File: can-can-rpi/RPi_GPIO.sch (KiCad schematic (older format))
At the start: 1 part, among them J2 RPi_GPIO

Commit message: wip
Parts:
- added C1, C2, C5, C6, C7: 100nF, Capacitors_ThroughHole:C_Disc_D3_P2.5, symbol C
- added C3, C4: 27pF, Capacitors_ThroughHole:C_Disc_D3_P2.5, symbol C
- added CON1: BARREL_JACK, Connect:BARREL_JACK, symbol BARREL_JACK
- added JP1: ICSP, ICSP:ICSP, symbol ICSP
- added JP2, JP3, JP4, JP5, JP6: JUMPER, Wire_Pads:SolderWirePad_2x_1mmDrill, symbol JUMPER
- added OC1, OC2: 6N137, Housings_DIP:DIP-8_W7.62mm, symbol 6N137
- added P1: CONN_02X02, Pin_Headers:Pin_Header_Straight_2x02, symbol CONN_02X02
- added P2, P3: CONN_01X14, Socket_Strips:Socket_Strip_Straight_1x14, symbol CONN_01X14
- added P5: CONN_01X03, Pin_Headers:Pin_Header_Straight_1x03, symbol CONN_01X03
- added R1: 15k, Resistors_ThroughHole:Resistor_Horizontal_RM10mm, symbol R
- added R10, R7, R8, R9: 390, Resistors_ThroughHole:Resistor_Horizontal_RM10mm, symbol R
- added R3, R4: 3k3, Resistors_ThroughHole:Resistor_Horizontal_RM10mm, symbol R
- added R5, R6: 470, Resistors_ThroughHole:Resistor_Horizontal_RM10mm, symbol R
- added U1: PIC18F25K80, Housings_DIP:DIP-28_W7.62mm, symbol PIC18F25K80
- added U2: MCP2562-I/P, Housings_DIP:DIP-8_W7.62mm_LongPads, symbol MCP2562-I/P
- added Y1: 16MHz, Crystals:Crystal_HC49-U_Vertical, symbol Crystal
- J1: renamed from J2; footprint RPi_Hat:Pin_Header_Straight_2x20 -> Socket_Strips:Socket_Strip_Straight_2x20
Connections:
- net labels added: +5V, CANRX, CANTX, GND, GNDA, PGC, PGD, RA0, RA1, RA2, RA3, RA5, RA6, RA7, RB0, RB1, RB4, RB5, RC0, RC1, RC2, RC5, RxD, SCL, SDA, TxD, VCC, VDD, _CANRX, _CANTX, ~MCLR
- wire segments 0 -> 174
- no-connect marks 0 -> 25
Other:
- note added: "Bypass galvanic isolation\n"
- moved on the sheet: J1

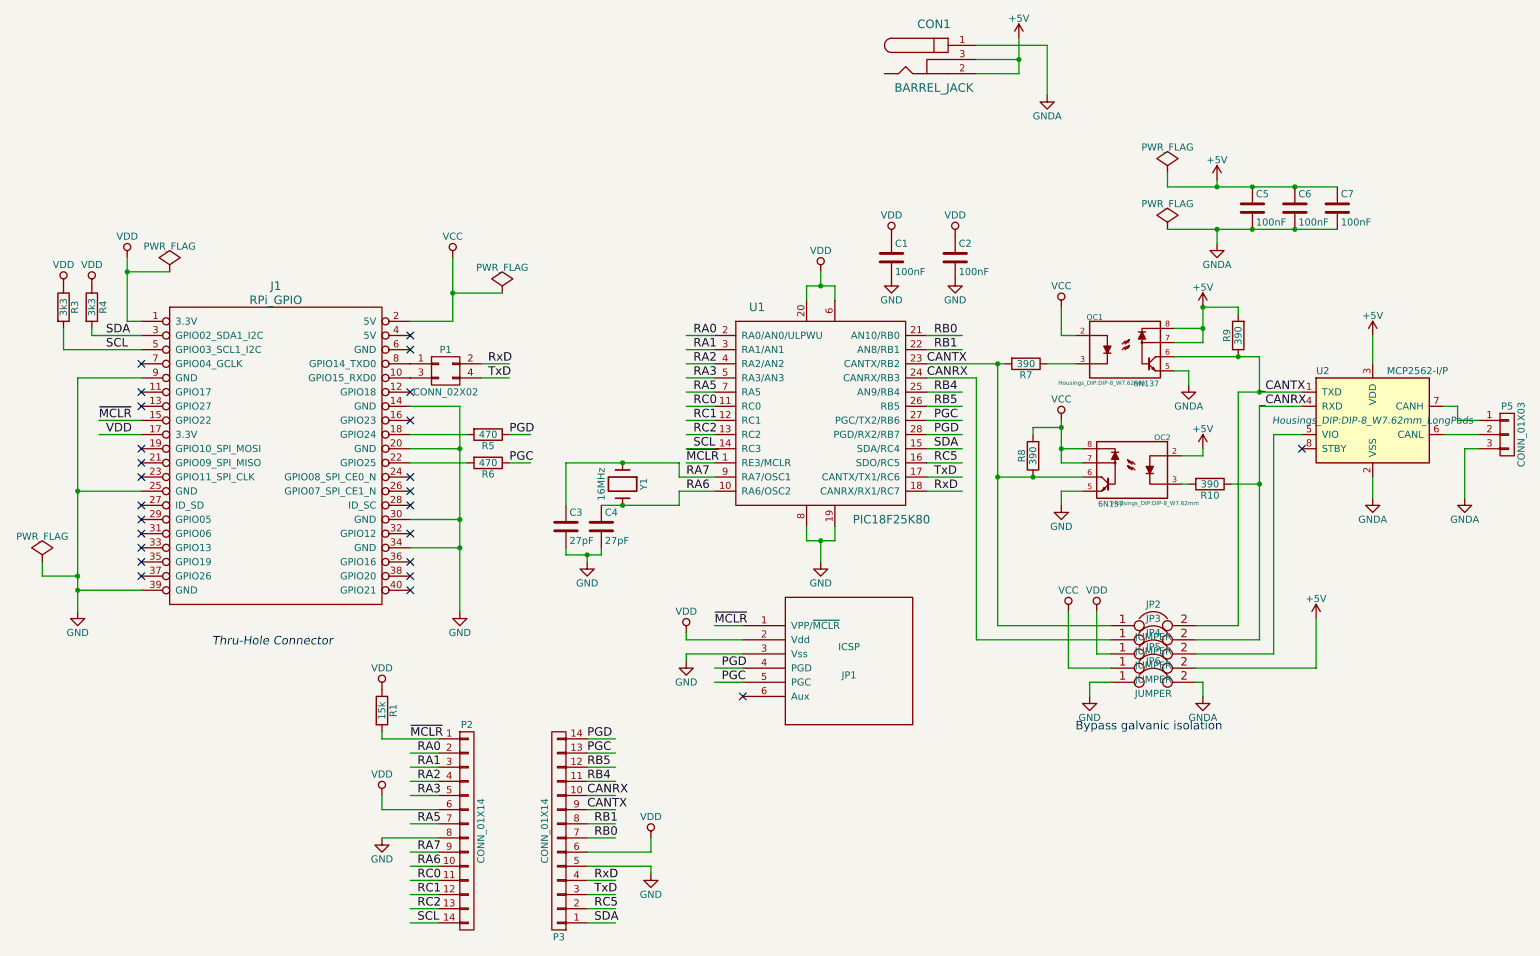
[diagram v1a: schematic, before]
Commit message: add LEDs and CTS
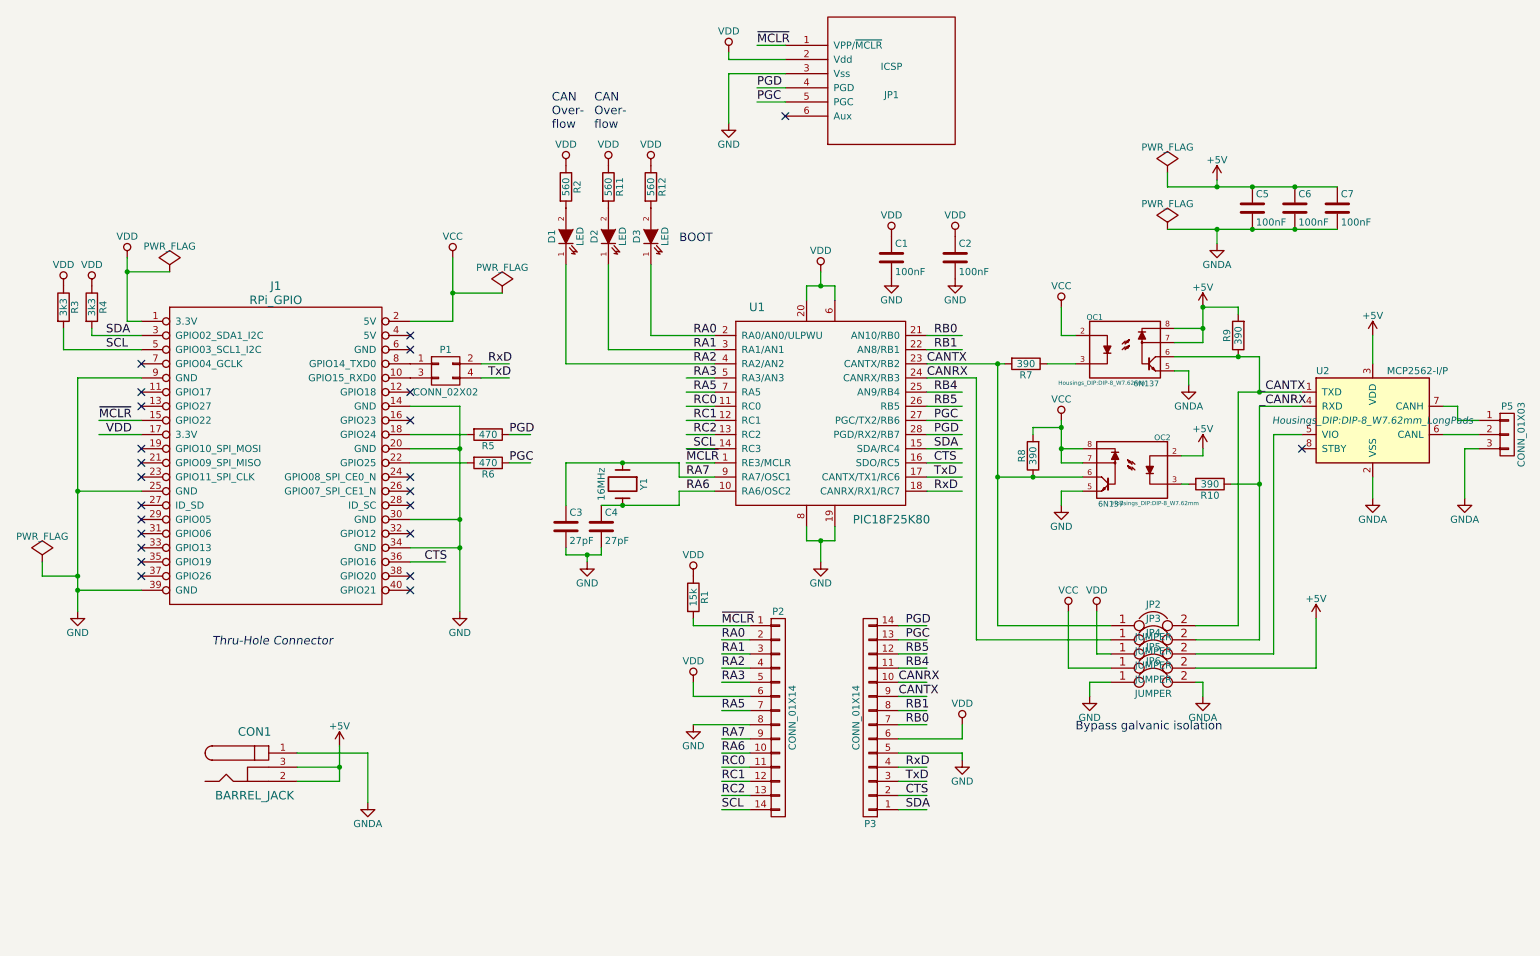
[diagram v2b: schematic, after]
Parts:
- added D1, D2, D3: LED, symbol LED
- added R11, R12, R2: 560, Resistors_ThroughHole:Resistor_Horizontal_RM10mm, symbol R
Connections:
- net labels added: CTS
- net labels removed: RC5
- wire segments 174 -> 178
- no-connect marks 25 -> 24
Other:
- note added: "BOOT"
- note added: "CAN\nOver-\nflow"
- moved on the sheet: CON1, JP1, P2, P3, R1

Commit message: update schematic and board
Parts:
- added P4: CONN_01X02, Pin_Headers:Pin_Header_Straight_1x02, symbol CONN_01X02
- added R13: 120, Resistors_ThroughHole:Resistor_Horizontal_RM10mm, symbol R
- added R14: 680, Resistors_ThroughHole:Resistor_Horizontal_RM10mm, symbol R
- D1, D2, D3: footprint (none) -> LEDs:LED-3MM
- R5, R6: value 470 -> 390
- R7: value 390 -> 180
- renumbered R2 to R12, R12 to R2
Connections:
- no-connect marks 24 -> 26
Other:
- moved on the sheet: R5, R6
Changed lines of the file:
@@
 EESchema Schematic File Version 2
+LIBS:RPi_Hat-rescue
 LIBS:power
 LIBS:device
@@
 $EndComp
 $Comp
-L GND #PWR01
+L GND-RESCUE-RPi_Hat #PWR01
 U 1 1 55BB6A0A
 P 6200 4550
+AR Path="/55BB6A0A" Ref="#PWR01"  Part="1"
+AR Path="/5515D395/55BB6A0A" Ref="#PWR01"  Part="1"
 F 0 "#PWR01" H 6200 4300 50  0001 C CNN
 F 1 "GND" H 6200 4400 50  0000 C CNN
@@
 $EndComp
 $Comp
-L GND #PWR03
+L GND-RESCUE-RPi_Hat #PWR03
 U 1 1 55BB6AF3
 P 6700 2550
+AR Path="/55BB6AF3" Ref="#PWR03"  Part="1"
+AR Path="/5515D395/55BB6AF3" Ref="#PWR03"  Part="1"
 F 0 "#PWR03" H 6700 2300 50  0001 C CNN
 F 1 "GND" H 6700 2400 50  0000 C CNN
@@
 $EndComp
 $Comp
-L GND #PWR05
+L GND-RESCUE-RPi_Hat #PWR05
 U 1 1 55BB6C16
 P 7150 2550
+AR Path="/55BB6C16" Ref="#PWR05"  Part="1"
+AR Path="/5515D395/55BB6C16" Ref="#PWR05"  Part="1"
 F 0 "#PWR05" H 7150 2300 50  0001 C CNN
 F 1 "GND" H 7150 2400 50  0000 C CNN
@@
 $EndComp
 $Comp
-L GND #PWR07
+L GND-RESCUE-RPi_Hat #PWR07
 U 1 1 55BB6F4C
 P 4550 4550
+AR Path="/55BB6F4C" Ref="#PWR07"  Part="1"
+AR Path="/5515D395/55BB6F4C" Ref="#PWR07"  Part="1"
 F 0 "#PWR07" H 4550 4300 50  0001 C CNN
 F 1 "GND" H 4550 4400 50  0000 C CNN
@@
 	1    0    0    -1
 $EndComp
-Text Label 3850 3150 0    60   ~ 0
-RxD
-Text Label 3850 3250 0    60   ~ 0
-TxD
 $Comp
 L 6N137 OC1
@@
 $EndComp
 $Comp
-L GND #PWR012
+L GND-RESCUE-RPi_Hat #PWR012
 U 1 1 55BBE7FB
 P 7200 5950
+AR Path="/55BBE7FB" Ref="#PWR012"  Part="1"
+AR Path="/5515D395/55BBE7FB" Ref="#PWR012"  Part="1"
 F 0 "#PWR012" H 7200 5700 50  0001 C CNN
 F 1 "GND" H 7200 5800 50  0000 C CNN
@@
 $EndComp
 $Comp
-L GND #PWR016
+L GND-RESCUE-RPi_Hat #PWR016
 U 1 1 55BC19FE
 P 5300 5700
+AR Path="/55BC19FE" Ref="#PWR016"  Part="1"
+AR Path="/5515D395/55BC19FE" Ref="#PWR016"  Part="1"
 F 0 "#PWR016" H 5300 5450 50  0001 C CNN
 F 1 "GND" H 5300 5550 50  0000 C CNN
@@
 $EndComp
 $Comp
-L GND #PWR019
+L GND-RESCUE-RPi_Hat #PWR019
 U 1 1 55BC3BB4
 P 3650 4900
+AR Path="/55BC3BB4" Ref="#PWR019"  Part="1"
+AR Path="/5515D395/55BC3BB4" Ref="#PWR019"  Part="1"
 F 0 "#PWR019" H 3650 4650 50  0001 C CNN
 F 1 "GND" H 3650 4750 50  0000 C CNN
@@
 $EndComp
 $Comp
-L GND #PWR020
+L GND-RESCUE-RPi_Hat #PWR020
 U 1 1 55BC413C
 P 950 4900
+AR Path="/55BC413C" Ref="#PWR020"  Part="1"
+AR Path="/5515D395/55BC413C" Ref="#PWR020"  Part="1"
 F 0 "#PWR020" H 950 4650 50  0001 C CNN
 F 1 "GND" H 950 4750 50  0000 C CNN
@@
 $EndComp
 $Comp
-L GNDA #PWR023
+L GNDA-RESCUE-RPi_Hat #PWR023
 U 1 1 55BC53DA
 P 8800 3300
@@
 $EndComp
 $Comp
-L GND #PWR024
+L GND-RESCUE-RPi_Hat #PWR024
 U 1 1 55BC634B
-P 7900 4150
-F 0 "#PWR024" H 7900 3900 50  0001 C CNN
-F 1 "GND" H 7900 4000 50  0000 C CNN
-F 2 "" H 7900 4150 60  0000 C CNN
-F 3 "" H 7900 4150 60  0000 C CNN
-	1    7900 4150
+P 7900 4350
+AR Path="/55BC634B" Ref="#PWR024"  Part="1"
+AR Path="/5515D395/55BC634B" Ref="#PWR024"  Part="1"
+F 0 "#PWR024" H 7900 4100 50  0001 C CNN
+F 1 "GND" H 7900 4200 50  0000 C CNN
+F 2 "" H 7900 4350 60  0000 C CNN
+F 3 "" H 7900 4350 60  0000 C CNN
+	1    7900 4350
 	1    0    0    -1
 $EndComp
@@
 P 7650 3150
 F 0 "R7" V 7730 3150 50  0000 C CNN
-F 1 "390" V 7650 3150 50  0000 C CNN
+F 1 "180" V 7650 3150 50  0000 C CNN
 F 2 "Resistors_ThroughHole:Resistor_Horizontal_RM10mm" V 7580 3150 30  0001 C CNN
 F 3 "" H 7650 3150 30  0000 C CNN
@@
 L R R6
 U 1 1 55BCA023
-P 3850 3850
-F 0 "R6" V 3930 3850 50  0000 C CNN
-F 1 "470" V 3850 3850 50  0000 C CNN
-F 2 "Resistors_ThroughHole:Resistor_Horizontal_RM10mm" V 3780 3850 30  0001 C CNN
-F 3 "" H 3850 3850 30  0000 C CNN
-	1    3850 3850
+P 3950 3250
+F 0 "R6" V 4030 3250 50  0000 C CNN
+F 1 "390" V 3950 3250 50  0000 C CNN
+F 2 "Resistors_ThroughHole:Resistor_Horizontal_RM10mm" V 3880 3250 30  0001 C CNN
+F 3 "" H 3950 3250 30  0000 C CNN
+	1    3950 3250
 	0    1    1    0
 $EndComp
@@
 L R R5
 U 1 1 55BCA133
-P 3850 3650
-F 0 "R5" V 3930 3650 50  0000 C CNN
-F 1 "470" V 3850 3650 50  0000 C CNN
-F 2 "Resistors_ThroughHole:Resistor_Horizontal_RM10mm" V 3780 3650 30  0001 C CNN
-F 3 "" H 3850 3650 30  0000 C CNN
-	1    3850 3650
+P 3950 3150
+F 0 "R5" V 4030 3150 50  0000 C CNN
+F 1 "390" V 3950 3150 50  0000 C CNN
+F 2 "Resistors_ThroughHole:Resistor_Horizontal_RM10mm" V 3880 3150 30  0001 C CNN
+F 3 "" H 3950 3150 30  0000 C CNN
+	1    3950 3150
 	0    1    1    0
 $EndComp
-Text Label 4000 3650 0    60   ~ 0
+Text Label 4100 3150 0    60   ~ 0
 PGD
-Text Label 4000 3850 0    60   ~ 0
+Text Label 4100 3250 0    60   ~ 0
 PGC
 NoConn ~ 1400 3150
@@
 $EndComp
 $Comp
-L GNDA #PWR030
+L GNDA-RESCUE-RPi_Hat #PWR030
 U 1 1 55BCF91F
 P 9000 2300
@@
 $EndComp
 $Comp
-L GNDA #PWR033
+L GNDA-RESCUE-RPi_Hat #PWR033
 U 1 1 55BB9FC1
 P 10100 4100
@@
 Bypass galvanic isolation\n
 $Comp
-L GNDA #PWR035
+L GNDA-RESCUE-RPi_Hat #PWR035
 U 1 1 55BBBB99
 P 8900 5500
@@
 $EndComp
 $Comp
-L GND #PWR036
+L GND-RESCUE-RPi_Hat #PWR036
 U 1 1 55BBBC10
 P 8100 5500
+AR Path="/55BBBC10" Ref="#PWR036"  Part="1"
+AR Path="/5515D395/55BBBC10" Ref="#PWR036"  Part="1"
 F 0 "#PWR036" H 8100 5250 50  0001 C CNN
 F 1 "GND" H 8100 5350 50  0000 C CNN
@@
 $EndComp
 $Comp
-L GNDA #PWR037
+L GNDA-RESCUE-RPi_Hat #PWR037
 U 1 1 55BBC07E
 P 10750 4100
@@
 	6950 3950 7200 3950
 Wire Wire Line
-	3800 3150 4000 3150
-Wire Wire Line
-	3800 3250 4000 3250
-Wire Wire Line
 	1300 2850 1400 2850
 Wire Wire Line
@@
 	8050 4050 7900 4050
 Wire Wire Line
-	7900 4050 7900 4150
+	7900 4050 7900 4350
 Wire Wire Line
 	7800 3150 8000 3150
@@
 Wire Wire Line
 	1400 3550 1100 3550
-Wire Wire Line
-	3300 3850 3700 3850
-Wire Wire Line
-	3300 3650 3700 3650
-Wire Wire Line
-	4000 3650 4150 3650
-Wire Wire Line
-	4000 3850 4150 3850
 Wire Wire Line
 	9000 1850 9000 1900
@@
 Connection ~ 7450 3950
 Wire Wire Line
-	10600 3450 10700 3450
-Wire Wire Line
-	10700 3450 10700 3550
-Wire Wire Line
-	10700 3550 10850 3550
+	10600 3450 10600 3450
+Wire Wire Line
+	10600 3450 10600 3550
+Wire Wire Line
+	10600 3550 10850 3550
 Wire Wire Line
 	10850 3650 10600 3650
@@
 $EndComp
 $Comp
-L GNDA #PWR041
+L GNDA-RESCUE-RPi_Hat #PWR041
 U 1 1 55BC0B5D
 P 3000 6250
@@
 $EndComp
 $Comp
-L R R2
+L R R12
 U 1 1 55BBD74B
 P 4400 1900
-F 0 "R2" V 4480 1900 50  0000 C CNN
+F 0 "R12" V 4480 1900 50  0000 C CNN
 F 1 "560" V 4400 1900 50  0000 C CNN
 F 2 "Resistors_ThroughHole:Resistor_Horizontal_RM10mm" V 4330 1900 30  0001 C CNN
@@
 F 0 "D1" H 4400 2350 50  0000 C CNN
 F 1 "LED" H 4400 2150 50  0000 C CNN
-F 2 "" H 4400 2250 60  0000 C CNN
+F 2 "LEDs:LED-3MM" H 4400 2250 60  0001 C CNN
 F 3 "" H 4400 2250 60  0000 C CNN
 	1    4400 2250
@@
 $EndComp
 $Comp
-L R R12
+L R R2
 U 1 1 55BBF02C
 P 5000 1900
-F 0 "R12" V 5080 1900 50  0000 C CNN
+F 0 "R2" V 5080 1900 50  0000 C CNN
 F 1 "560" V 5000 1900 50  0000 C CNN
 F 2 "Resistors_ThroughHole:Resistor_Horizontal_RM10mm" V 4930 1900 30  0001 C CNN
@@
 F 0 "D2" H 4700 2350 50  0000 C CNN
 F 1 "LED" H 4700 2150 50  0000 C CNN
-F 2 "" H 4700 2250 60  0000 C CNN
+F 2 "LEDs:LED-3MM" H 4700 2250 60  0001 C CNN
 F 3 "" H 4700 2250 60  0000 C CNN
 	1    4700 2250
@@
 F 0 "D3" H 5000 2350 50  0000 C CNN
 F 1 "LED" H 5000 2150 50  0000 C CNN
-F 2 "" H 5000 2250 60  0000 C CNN
+F 2 "LEDs:LED-3MM" H 5000 2250 60  0001 C CNN
 F 3 "" H 5000 2250 60  0000 C CNN
 	1    5000 2250
@@
 CTS
 $Comp
-L GND #PWR046
+L GND-RESCUE-RPi_Hat #PWR046
 U 1 1 55BC2E99
 P 5550 1450
+AR Path="/55BC2E99" Ref="#PWR046"  Part="1"
+AR Path="/5515D395/55BC2E99" Ref="#PWR046"  Part="1"
 F 0 "#PWR046" H 5550 1200 50  0001 C CNN
 F 1 "GND" H 5550 1300 50  0000 C CNN
@@
 	1    0    0    -1
 $EndComp
+$Comp
+L CONN_01X02 P4
+U 1 1 55BBFA9F
+P 10800 2650
+F 0 "P4" H 10800 2800 50  0000 C CNN
+F 1 "CONN_01X02" V 10900 2650 50  0000 C CNN
+F 2 "Pin_Headers:Pin_Header_Straight_1x02" H 10800 2650 60  0001 C CNN
+F 3 "" H 10800 2650 60  0000 C CNN
+	1    10800 2650
+	0    -1   -1   0
+$EndComp
+$Comp
+L R R13
+U 1 1 55BBFB57
+P 10850 3100
+F 0 "R13" V 10930 3100 50  0000 C CNN
+F 1 "120" V 10850 3100 50  0000 C CNN
+F 2 "Resistors_ThroughHole:Resistor_Horizontal_RM10mm" V 10780 3100 30  0001 C CNN
+F 3 "" H 10850 3100 30  0000 C CNN
+	1    10850 3100
+	-1   0    0    1
+$EndComp
+Wire Wire Line
+	10850 2950 10850 2850
+Wire Wire Line
+	10850 3250 10850 3650
+Connection ~ 10850 3650
+Wire Wire Line
+	10750 2850 10750 3550
+Connection ~ 10750 3550
+Connection ~ 9700 4350
+$Comp
+L R R14
+U 1 1 55BFF952
+P 7700 4100
+F 0 "R14" V 7780 4100 50  0000 C CNN
+F 1 "680" V 7700 4100 50  0000 C CNN
+F 2 "Resistors_ThroughHole:Resistor_Horizontal_RM10mm" V 7630 4100 30  0001 C CNN
+F 3 "" H 7700 4100 30  0000 C CNN
+	1    7700 4100
+	-1   0    0    1
+$EndComp
+Wire Wire Line
+	7700 4250 7900 4250
+Connection ~ 7900 4250
+NoConn ~ 3300 3650
+NoConn ~ 3300 3850
+Wire Wire Line
+	4100 3150 4300 3150
+Wire Wire Line
+	4100 3250 4300 3250
 $EndSCHEMATC

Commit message: change footprints and layout - wip
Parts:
- C3, C4: value 27pF -> 22pF
- JP2, JP3, JP4, JP5, JP6: footprint Wire_Pads:SolderWirePad_2x_1mmDrill -> Wire_Pads:SolderWirePad_2x_0-2.54mmDrill
- R1: value 15k -> 4.7k
- R7: value 180 -> 390
- renumbered D3 to D1, D1 to D3
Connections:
- wire segments 178 -> 174
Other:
- note added: "SYSTEM"
- note removed: "BOOT"
- moved on the sheet: R10, R7
